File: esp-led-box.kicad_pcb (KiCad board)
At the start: 2 copper layers, 41 x 66 mm, 38 parts, among them J1 Conn_01x03, J2 Conn_01x03_Female, J3 Conn_01x02_Female, Q1 BSS138, U1 MP2307, U2 LM3940, U3 ESP-12F

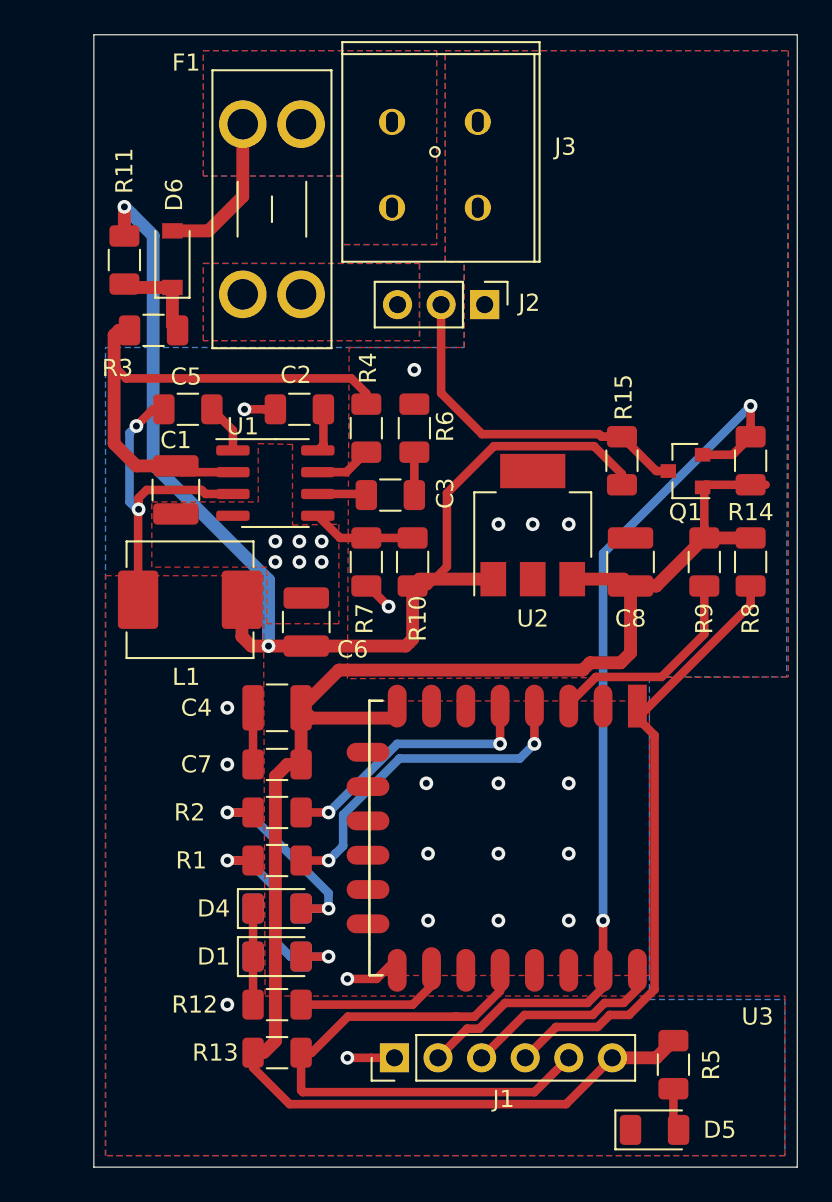
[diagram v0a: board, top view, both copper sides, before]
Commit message: rework fuse holder: use one from aliexpress
https://aliexpress.ru/item/32838425418.html?spm=a2g0s.9042311.0.0.5f9933edQqCEM1 here is the link (it supposed to be used with micro blades fuses)
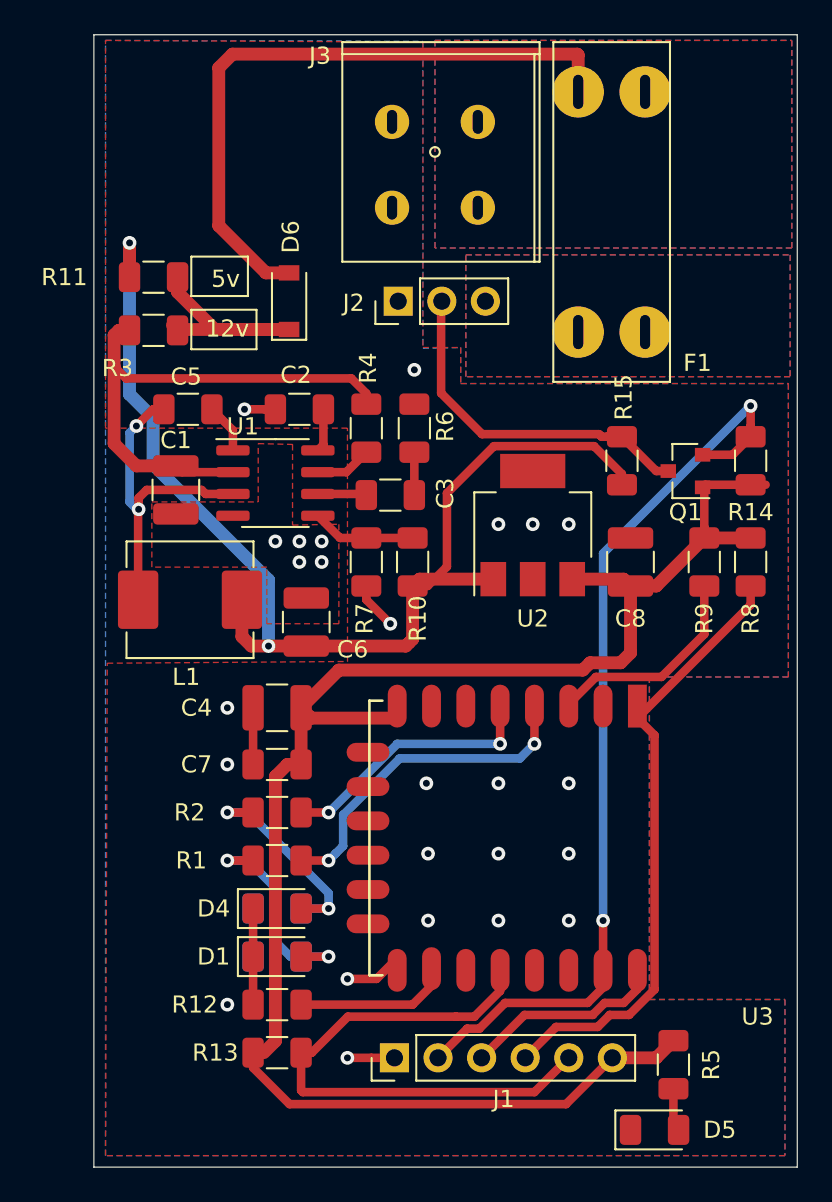
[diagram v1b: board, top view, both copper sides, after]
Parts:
- F1: footprint Fuse:Fuseholder_Blade_Mini_Keystone_3568 -> esp-light-box:fuseholder_blade_common_aliexpress
- moved F1 18.7 mm to (137.7, 60.3)
- moved D6 7.23 mm to (122.4, 55.5)
- moved J2 5.04 mm to (128.8, 55.5), turned to 90 degrees
- moved R11 1.97 mm to (114.5, 54.1), turned to 180 degrees
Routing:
- net VSS: track 9.15 -> 37.9 mm
- net +VDC: track 5.51 -> 15.2 mm
- net +5V: track 70.6 -> 68.7 mm
- net GND: track 18.6 -> 19.7 mm, vias 26 -> 25
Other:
- board text added: "12v"
- board text added: "5v"

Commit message: pcb v0.3 update
- add possibility to use switch instead of dummy resisters
- add micro USB footprint for portable use
- add buttons for RESET and GPIO0 ESP inputs
- make it fancier with components density increased
- add case mountpoints
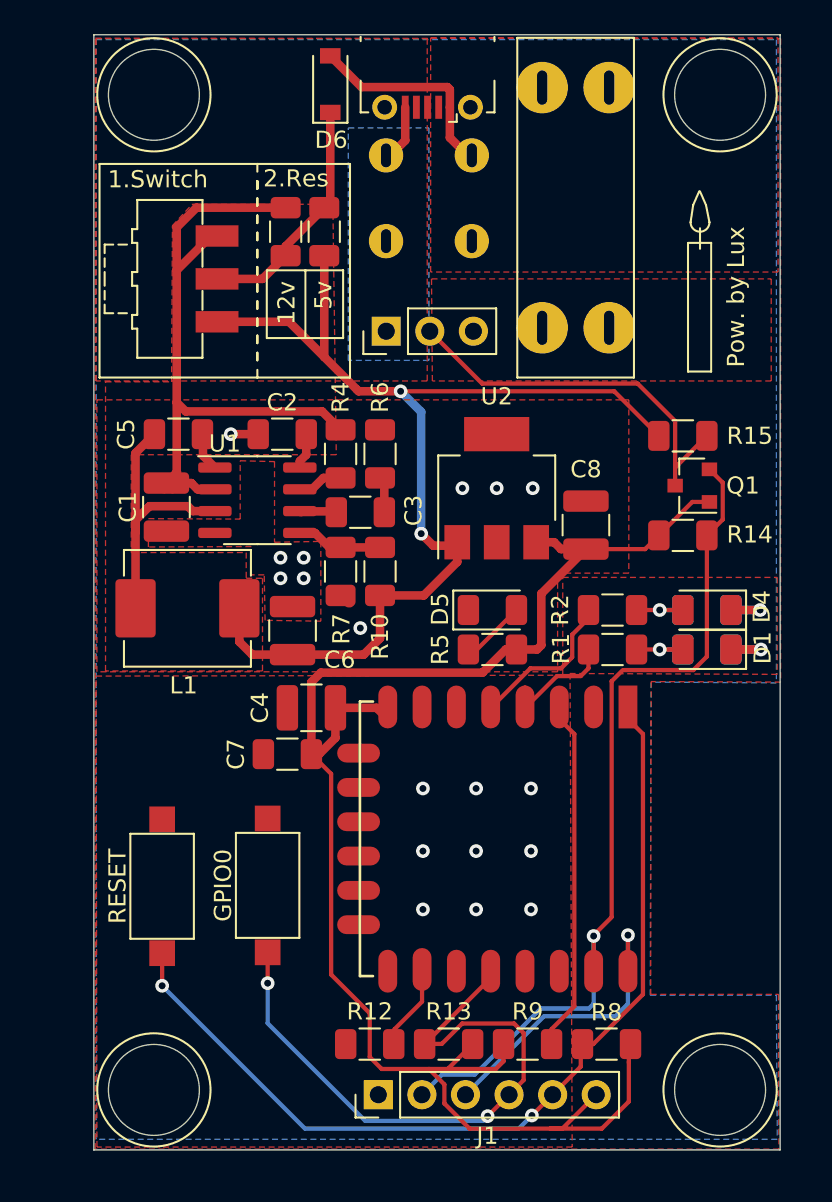
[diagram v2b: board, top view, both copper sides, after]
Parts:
- added GPIO0: SW_Push, Button_Switch_SMD:SW_SPST_CK_RS282G05A3, F.Cu at (121.2, 89.5)
- added J4: USB_B_Micro, Connector_USB:USB_Micro-B_Molex-105017-0001, F.Cu at (130.5, 42.7)
- added REF**: MountingHole_5.3mm_M5, MountingHole:MountingHole_5.3mm_M5, F.Cu at (147.5, 101.5)
- added REF**: MountingHole_5.3mm_M5, MountingHole:MountingHole_5.3mm_M5, F.Cu at (147.5, 43.5)
- added REF**: MountingHole_5.3mm_M5, MountingHole:MountingHole_5.3mm_M5, F.Cu at (114.5, 101.5)
- added REF**: MountingHole_5.3mm_M5, MountingHole:MountingHole_5.3mm_M5, F.Cu at (114.5, 43.5)
- added RESET: SW_Push, Button_Switch_SMD:SW_SPST_CK_RS282G05A3, F.Cu at (115.0, 89.6)
- added SW3: SW_SPDT, Button_Switch_SMD:SW_SPDT_CK-JS102011SAQN, F.Cu at (115.5, 54.2)
- J3: moved to B.Cu
- moved D5 31.7 mm to (134.2, 73.5)
- moved D1 30.8 mm to (146.8, 75.8), turned to 180 degrees
- moved D2 30.8 mm to (146.8, 75.8), turned to 180 degrees
- moved D3 30.5 mm to (146.8, 73.5), turned to 180 degrees
- moved D4 30.5 mm to (146.8, 73.5), turned to 180 degrees
- moved R9 29.9 mm to (136.3, 98.8), turned to 180 degrees
- moved R8 29.3 mm to (140.9, 98.8), turned to 0 degrees
- moved R5 26.4 mm to (134.2, 75.8), turned to 180 degrees
- moved R1 23.1 mm to (141.2, 75.8), turned to 0 degrees
- moved R2 22.8 mm to (141.2, 73.5), turned to 0 degrees
- moved D6 12.9 mm to (124.8, 42.9)
- moved J3 10.6 mm to (135.9, 55.1)
- moved R11 10.3 mm to (124.5, 51.5), turned to 270 degrees
- moved R13 10.0 mm to (131.7, 98.8), turned to 180 degrees
- moved R3 9.61 mm to (122.2, 51.5), turned to 90 degrees
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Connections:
- net Net-(C1-Pad1) renamed +12V
- J1 pad 4: /RESET -> /GPIO0
- J1 pad 5: /GPIO0 -> /RESET
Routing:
- net VSS: track 37.9 -> 12.4 mm
- net /RESET: track 35.9 -> 53.7 mm, vias 0 -> 2
- net /GREEN_LED: track 19.0 -> 8.25 mm, vias 2 -> 0
- net +12V: track 30.9 -> 40.9 mm
- net Net-(D3-Pad2): track 13.4 -> 4.05 mm, vias 2 -> 1
- net Net-(D1-Pad2): track 13.2 -> 4.05 mm, vias 2 -> 1
- net GND: track 19.7 -> 12.1 mm, vias 25 -> 20
- net Net-(R9-Pad1): track 13.2 -> 19.9 mm
- net /GPIO0: track 33.7 -> 39.3 mm, vias 0 -> 2
- net /TXD: track 12.5 -> 17.1 mm, vias 0 -> 1
- net /RED_LED: track 14.8 -> 10.7 mm, vias 2 -> 0
- net Net-(R12-Pad2): track 9.66 -> 5.61 mm
- net +3V3: track 99.2 -> 95.5 mm
- net +5V: track 68.7 -> 65.5 mm
- net Net-(C5-Pad1): track 19.0 -> 16.4 mm, vias 2 -> 0
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- added copper zone on F.Cu, net (none)
- removed copper zone on B.Cu, net Net-(F1-Pad1)
- removed copper zone on B.Cu, net VSS
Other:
- board size 41 x 66 mm -> 40 x 65 mm
- board text added: "1.Switch"
- board text added: "2.Res"
- board text added: "Pow. by Lux"

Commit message: my new version is coming
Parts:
- removed D2, D3, D4, D5: LED, LED_SMD:LED_1206_3216Metric
- removed D6: D, Diode_SMD:D_SOD-123
- removed GPIO0, RESET: SW_Push, Button_Switch_SMD:SW_SPST_CK_RS282G05A3
- removed the REF** at (147.5, 101.5)
- removed the REF** at (147.5, 43.5)
- removed the REF** at (114.5, 101.5)
- removed the REF** at (114.5, 43.5)
- removed SW3: SW_SPDT, Button_Switch_SMD:SW_SPDT_CK-JS102011SAQN
- added C10: 1uF, Capacitor_SMD:C_0402_1005Metric, F.Cu at (163.4, 68.8)
- added C11: 220u, Capacitor_SMD:CP_Elec_6.3x7.7, F.Cu at (138.4, 82.8)
- added C12: 100nF, Capacitor_SMD:C_0402_1005Metric, F.Cu at (162.4, 68.8)
- added C9: 10u, Capacitor_SMD:C_0603_1608Metric, F.Cu at (157.4, 60.8)
- added IC1: CP2105-F01-GMR, CP2105-F01-GMR:QFN50P400X400X80-25N-D, F.Cu at (160.4, 66.3)
- added J5: Conn_01x02, Connector_PinHeader_2.54mm:PinHeader_1x02_P2.54mm_Vertical, F.Cu at (128.2, 105.2)
- added Q2: Q_PMOS_DGS, Package_TO_SOT_SMD:SOT-23-6, F.Cu at (161.0, 85.3)
- added Q3: Q_PMOS_DGS, Package_TO_SOT_SMD:SOT-23-6, F.Cu at (154.2, 99.0)
- added Q4: S8050, Package_TO_SOT_SMD:SOT-23, F.Cu at (157.1, 70.0)
- added Q5: S8050, Package_TO_SOT_SMD:SOT-23, F.Cu at (153.6, 70.0)
- added Q6: Q_PMOS_DGS, Package_TO_SOT_SMD:SOT-23-6, F.Cu at (153.6, 66.0)
- added Q7: BSS138, Package_TO_SOT_SMD:SOT-23, F.Cu at (138.8, 96.2)
- added Q8: Q_PMOS_DGS, Package_TO_SOT_SMD:TO-252-2, F.Cu at (140.6, 73.6)
- added Q9: Q_NMOS, Package_TO_SOT_SMD:SOT-23, F.Cu at (145.7, 64.2)
- added R16: 20K, Resistor_SMD:R_0402_1005Metric, F.Cu at (157.1, 73.7)
- added R17: 12K, Resistor_SMD:R_0402_1005Metric, F.Cu at (156.9, 67.4)
- added R18: 12K, Resistor_SMD:R_0402_1005Metric, F.Cu at (156.9, 64.5)
- added R21: 4.7K, Resistor_SMD:R_0402_1005Metric, F.Cu at (163.4, 66.0)
- added R22: 300, Resistor_SMD:R_0402_1005Metric, F.Cu at (156.9, 66.5)
- added R23: 300, Resistor_SMD:R_0402_1005Metric, F.Cu at (156.9, 65.5)
- added R24: 10K, Resistor_SMD:R_0402_1005Metric, F.Cu at (138.3, 98.5)
- added R25: 10K, Resistor_SMD:R_0402_1005Metric, F.Cu at (141.5, 95.0)
- added REF**: MountingHole_2.2mm_M2, MountingHole:MountingHole_2.2mm_M2, F.Cu at (162.0, 60.5)
- added REF**: MountingHole_2.2mm_M2, MountingHole:MountingHole_2.2mm_M2, F.Cu at (128.0, 60.5)
- added REF**: MountingHole_2.2mm_M2, MountingHole:MountingHole_2.2mm_M2, F.Cu at (128.0, 119.5)
- added REF**: MountingHole_2.2mm_M2, MountingHole:MountingHole_2.2mm_M2, F.Cu at (162.0, 119.5)
- added U4: LM3940, Package_TO_SOT_SMD:SOT-223-3_TabPin2, F.Cu at (147.1, 97.2)
- C1: value 10uF/25V -> 10u/25V; footprint Capacitor_SMD:C_1210_3225Metric -> Capacitor_SMD:C_1206_3216Metric
- C2: value 0.1uF -> 10uF; footprint Capacitor_SMD:C_1206_3216Metric -> Capacitor_Tantalum_SMD:CP_EIA-3216-18_Kemet-A
- C3: value 3.9nF -> 100nF; footprint Capacitor_SMD:C_1206_3216Metric -> Capacitor_SMD:C_0402_1005Metric
- C4: value 10uF -> 100nF; footprint Capacitor_SMD:C_1210_3225Metric -> Capacitor_SMD:C_0402_1005Metric
- C5: value 10nF -> 3.9nF; footprint Capacitor_SMD:C_1206_3216Metric -> Capacitor_SMD:C_0402_1005Metric
- C6: value 22uF/6.3V -> 10nF; footprint Capacitor_SMD:C_1210_3225Metric -> Capacitor_SMD:C_0402_1005Metric
- C7: value 100nF -> 47uF/6.3V
- C8: footprint Capacitor_SMD:C_1210_3225Metric -> Capacitor_Tantalum_SMD:CP_EIA-3216-18_Kemet-A
- D1: value LED -> 2.4V; footprint LED_SMD:LED_1206_3216Metric -> Diode_SMD:D_SOD-323
- J1: value Conn_01x03 -> Conn_01x04; footprint Connector_PinHeader_2.54mm:PinHeader_1x06_P2.54mm_Vertical -> Connector_PinHeader_2.54mm:PinHeader_1x04_P2.54mm_Vertical
- J2: value Conn_01x03_Female -> USB_B_Micro; footprint Connector_PinHeader_2.54mm:PinHeader_1x03_P2.54mm_Vertical -> Connector_USB:USB_Micro-B_Molex-105017-0001
- J3: value Conn_01x02_Female -> Conn_01x03_Female; footprint esp-light-box:WG235-2P -> esp-light-box:SolderWire_1x03_2.5x6; moved to F.Cu
- J4: value USB_B_Micro -> Conn_01x03_Female; footprint Connector_USB:USB_Micro-B_Molex-105017-0001 -> esp-light-box:SolderWire_1x03_2.5x6
- L1: footprint Inductor_SMD:L_Abracon_ASPI-0630LR -> Inductor_SMD:L_Sunlord_MWSA0518_5.4x5.2mm
- Q1: value BSS138 -> Q_NMOS
- R1, R2: value 120 -> 1M; footprint Resistor_SMD:R_1206_3216Metric -> Resistor_SMD:R_0402_1005Metric
- R10, R12, R4: footprint Resistor_SMD:R_1206_3216Metric -> Resistor_SMD:R_0402_1005Metric
- R11: value 0 -> 360; footprint Resistor_SMD:R_1206_3216Metric -> Resistor_SMD:R_1210_3225Metric
- R13: value 10K -> 24K; footprint Resistor_SMD:R_1206_3216Metric -> Resistor_SMD:R_0603_1608Metric
- R14: footprint Resistor_SMD:R_1206_3216Metric -> Resistor_SMD:R_0603_1608Metric
- R15: value 10K -> 20K; footprint Resistor_SMD:R_1206_3216Metric -> Resistor_SMD:R_0402_1005Metric
- R3: value 0 -> 10K; footprint Resistor_SMD:R_1206_3216Metric -> Resistor_SMD:R_0402_1005Metric
- R5: value 120 -> 20K; footprint Resistor_SMD:R_1206_3216Metric -> Resistor_SMD:R_0603_1608Metric
- R6: value 6.8K -> 300; footprint Resistor_SMD:R_1206_3216Metric -> Resistor_SMD:R_0805_2012Metric
- R7: value 10K/1% -> 20K; footprint Resistor_SMD:R_1206_3216Metric -> Resistor_SMD:R_0603_1608Metric
- R8: value 10K -> 6.8K; footprint Resistor_SMD:R_1206_3216Metric -> Resistor_SMD:R_0402_1005Metric
- R9: value 10K -> 10K/1%; footprint Resistor_SMD:R_1206_3216Metric -> Resistor_SMD:R_0402_1005Metric
- U2: value LM3940 -> ESP-12F; footprint Package_TO_SOT_SMD:SOT-223-3_TabPin2 -> RF_Module:ESP-12E
- U3: value ESP-12F -> LM211; footprint ESP8266:ESP-12E -> Package_SO:SOIC-8-1EP_3.9x4.9mm_P1.27mm_EP2.29x3mm
- moved C5 57.1 mm to (159.7, 99.9), turned to 270 degrees
- moved R3 52.7 mm to (138.2, 101.7), turned to 270 degrees
- moved R4 50.1 mm to (160.8, 99.9), turned to 90 degrees
- moved C1 49.5 mm to (159.2, 90.3), turned to 180 degrees
- moved U1 48.1 mm to (159.6, 95.1), turned to 270 degrees
- moved C3 47.7 mm to (161.8, 99.9), turned to 270 degrees
- moved J4 47.4 mm to (138.5, 89.5), turned to 0 degrees
- moved U2 46.6 mm to (144.4, 111.9), turned to 270 degrees
- moved R11 43.2 mm to (160.7, 74.8), turned to 0 degrees
- moved C6 42.4 mm to (162.1, 90.4), turned to 270 degrees
- moved L1 41.1 mm to (155.6, 86.2), turned to 180 degrees
- moved C2 40.8 mm to (135.3, 101.8), turned to 0 degrees
- moved R10 40.7 mm to (156.6, 99.9), turned to 270 degrees
- moved J1 36.0 mm to (161.8, 112.8), turned to 180 degrees
- moved R13 35.4 mm to (162.1, 80.5), turned to 90 degrees
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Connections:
- C2 pad 1: Net-(C2-Pad1) -> +3V3
- C3 pad 2: Net-(C3-Pad2) -> GND
- C6 pad 1: +5V -> Net-(C6-Pad1)
- C6 pad 2: GND -> Net-(C6-Pad2)
- C7 pad 1: +3V3 -> /BUCK_5V
- D1 pad 1: GND -> Net-(D1-Pad1)
- D1 pad 2: Net-(D1-Pad2) -> GND
- F1 pad 1: Net-(F1-Pad1) -> /DC_VDD
- F1 pad 2: VSS -> VDD
- J1 pad 1: GND -> /GPIO0
- J1 pad 2: /RXD|CONTROL -> /TXD
- J1 pad 3: /TXD -> /RXD
- J1 pad 4: /GPIO0 -> /RESET
- J2 pad 1: GND -> VBUS
- J2 pad 2: Net-(J2-Pad2) -> /D-
- J2 pad 3: Net-(F1-Pad1) -> /D+
- J3 pad 1: GND -> VDC
- J3 pad 2: VSS -> VDC
- J4 pad 1: VSS -> GND
- J4 pad 3: Net-(J4-Pad3) -> VDD
- L1 pad 1: Net-(C5-Pad1) -> Net-(C6-Pad1)
- L1 pad 2: +5V -> /BUCK_5V
- Q1 pad 1: +3V3 -> /~12V_SEL
- Q1 pad 2: /RXD|CONTROL -> GND
- Q1 pad 3: Net-(J2-Pad2) -> /~5V_SEL
- R1 pad 1: /GREEN_LED -> VBUS
- R1 pad 2: Net-(D1-Pad2) -> GND
- R10 pad 1: +5V -> /BUCK_5V
- R11 pad 1: +VDC -> Net-(D1-Pad1)
- R11 pad 2: +5V -> VDD
- R12 pad 1: GND -> Net-(R12-Pad1)
- R12 pad 2: Net-(R12-Pad2) -> GND
- R13 pad 1: +3V3 -> VDD
- R13 pad 2: /GPIO0 -> Net-(R13-Pad2)
- R14 pad 1: /RXD|CONTROL -> Net-(R13-Pad2)
- R14 pad 2: +3V3 -> GND
- R15 pad 1: Net-(J2-Pad2) -> VDD
- R15 pad 2: +5V -> /~12V_SEL
- R2 pad 1: /RED_LED -> VDC
- R2 pad 2: Net-(D3-Pad2) -> GND
- R3 pad 1: +VDC -> +3V3
- R3 pad 2: +12V -> Net-(R3-Pad2)
- R5 pad 1: +3V3 -> VBUS
- R5 pad 2: Net-(D5-Pad2) -> /~VDC_SEL
- R6 pad 1: Net-(C3-Pad2) -> VDC
- R6 pad 2: GND -> /VDC_ON
- R7 pad 1: Net-(R10-Pad2) -> VDC
- R7 pad 2: GND -> Net-(Q9-Pad1)
- R8 pad 1: /RESET -> Net-(C5-Pad2)
- R8 pad 2: +3V3 -> GND
- R9 pad 1: Net-(R9-Pad1) -> Net-(R10-Pad2)
- R9 pad 2: +3V3 -> GND
- U1 pad 1: Net-(C5-Pad2) -> Net-(C6-Pad2)
- U1 pad 3: Net-(C5-Pad1) -> Net-(C6-Pad1)
- U1 pad 6: Net-(C3-Pad1) -> Net-(C5-Pad1)
- U1 pad 8: Net-(C2-Pad1) -> Net-(C3-Pad1)
- U2 pad 1: +5V -> /RESET
- U2 pad 2: GND -> Net-(U2-Pad2)
- U2 pad 3: +3V3 -> Net-(R3-Pad2)
- U3 pad 1: /RESET -> GND
- U3 pad 2: Net-(U3-Pad2) -> Net-(R13-Pad2)
- U3 pad 3: Net-(R9-Pad1) -> Net-(D1-Pad1)
- U3 pad 4: /GREEN_LED -> GND
- U3 pad 5: /RED_LED -> Net-(U3-Pad5)
- U3 pad 6: Net-(U3-Pad6) -> Net-(U3-Pad5)
- U3 pad 7: Net-(U3-Pad7) -> /~12V_SEL
- U3 pad 8: +3V3 -> VDD
- U3 pad 9: GND -> (no net)
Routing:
- net /RXD: track 0.00 -> 76.9 mm, vias 0 -> 4
- net +3V3: track 95.5 -> 33.5 mm, vias 0 -> 1
- net /TXD: track 17.1 -> 74.6 mm, vias 1 -> 2
- net /RXD|CONTROL: track 52.2 -> 0.00 mm, vias 1 -> 0
- net /~5V_SEL: track 0.00 -> 51.2 mm
- net +5V: track 65.5 -> 17.4 mm, vias 2 -> 0
- net /GPIO0: track 39.3 -> 77.2 mm
- net /~12V_SEL: track 0.00 -> 37.5 mm, vias 0 -> 2
- net /LED_CTRL: track 0.00 -> 35.3 mm
- net VDD: track 0.00 -> 35.2 mm, vias 0 -> 25
- net VBUS: track 0.00 -> 30.4 mm
- net /DC_5V: track 0.00 -> 24.5 mm
- net Net-(J2-Pad2): track 22.8 -> 0.00 mm
- net +12V: track 40.9 -> 18.3 mm
- net /~VDC_SEL: track 0.00 -> 22.3 mm
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- added copper zone on B.Cu, net (none)
- added copper zone on F.Cu, net +12V
- added copper zone on F.Cu, net /BUCK_5V
- added copper zone on B.Cu, net /DC_VDD
- added copper zone on F.Cu, net /DC_VDD
- added copper zone on F.Cu, net Net-(C6-Pad1)
- added copper zone on B.Cu, net VDC
- added copper zone on F.Cu, net VDC
- added copper zone on B.Cu, net VDD
- added copper zone on F.Cu, net VDD
- removed copper zone on F.Cu, net Net-(F1-Pad1)
- removed copper zone on F.Cu, net VSS
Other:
- board size 40 x 65 mm -> 39 x 64 mm
- net class Default: clearance 0.2 -> 0.127; trace_width 0.25 -> 0.127
- net class Digital Power added: clearance 0.127, trace_width 0.254, via_dia 0.8, via_drill 0.4
- net class Signal added: clearance 0.127, trace_width 0.254, via_dia 0.8, via_drill 0.4
- rule trace_clearance: 0.2 -> 0.127
- rule trace_min: 0.2 -> 0.127
- rule via_min_drill: 0.3 -> 0.2
- board text removed: "1.Switch"
- board text removed: "12v"
- board text removed: "2.Res"
- board text removed: "5v"

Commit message: another kek
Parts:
- removed REF** (x4): MountingHole_2.2mm_M2, MountingHole:MountingHole_2.2mm_M2
- moved J1 77.2 mm to (86.4, 96.9), turned to 0 degrees
- moved C6 75.9 mm to (86.6, 82.4)
- moved C7 75.9 mm to (79.1, 82.3)
- moved C9 75.9 mm to (81.9, 52.8)
- moved Q5 75.9 mm to (78.1, 62.0)
- moved R13 75.9 mm to (86.6, 72.5)
- moved R2 75.9 mm to (69.7, 52.5)
- moved R5 75.9 mm to (74.1, 58.9)
- moved U3 75.9 mm to (80.6, 71.3)
- moved C1 75.9 mm to (83.7, 82.3)
- moved C10 75.9 mm to (87.9, 60.8)
- moved C11 75.9 mm to (62.9, 74.8)
- moved C12 75.9 mm to (86.9, 60.8)
- moved C2 75.9 mm to (59.9, 93.8)
- moved C4 75.9 mm to (58.6, 92.3)
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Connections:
- J1 pad 2: /TXD -> /RESET
- J1 pad 4: /RESET -> /TXD
- J5 pad 1: +3V3 -> GND
- J5 pad 2: GND -> +3V3
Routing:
- net +3V3: track 33.5 -> 24.8 mm, vias 1 -> 2
- net /V_IO: track 9.31 -> 15.0 mm
- net /RESET: track 59.5 -> 65.2 mm, vias 4 -> 0
- net /~5V_SEL: track 51.2 -> 47.3 mm, vias 0 -> 3
- net GND: track 30.6 -> 26.8 mm
- net VDD: track 35.2 -> 37.4 mm, vias 25 -> 27
- net /GPIO0: track 77.2 -> 79.5 mm, vias 2 -> 0
- net /TXD: track 74.6 -> 73.0 mm, vias 2 -> 1
- net /RXD: track 76.9 -> 75.5 mm, vias 4 -> 3
- net /D-: track 14.1 -> 13.0 mm
- net /D+: track 15.2 -> 14.2 mm
- added copper zone on B.Cu, net +3V3
- added copper zone on F.Cu, net +3V3
- added copper zone on F.Cu, net +5V
- removed copper zone on B.Cu, net (none)
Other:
- outline, holes or cut-outs redrawn

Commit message: another kek hehe
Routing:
- net /TXD: track 73.0 -> 90.7 mm, vias 1 -> 2
- net /RXD: track 75.5 -> 89.9 mm, vias 3 -> 2
- net Net-(R12-Pad1): track 19.4 -> 22.5 mm
- net /GPIO0: track 79.5 -> 79.0 mm

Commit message: finally we are done
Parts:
- removed the C10 at (87.9, 60.8)
- removed the C2 at (59.9, 93.8)
- removed the C5 at (84.2, 91.9)
- removed R24: 10K, Resistor_SMD:R_0402_1005Metric
- removed the U2 at (68.9, 103.9)
- removed the U4 at (71.6, 89.3)
- added C11: 1uF, Capacitor_SMD:C_0402_1005Metric, F.Cu at (87.9, 60.8)
- added C3: 3.9nF, Capacitor_SMD:C_0402_1005Metric, F.Cu at (84.2, 91.9)
- added C6: 100nF, Capacitor_SMD:C_0402_1005Metric, F.Cu at (56.9, 93.4)
- added R22: 10K, Resistor_SMD:R_0402_1005Metric, F.Cu at (56.7, 86.8)
- added REF**: TestPoint_Pad_4.0x4.0mm, TestPoint:TestPoint_Pad_4.0x4.0mm, B.Cu at (84.2, 71.3)
- added REF**: MountingHole_2.2mm_M2, MountingHole:MountingHole_2.2mm_M2, F.Cu at (52.5, 52.5)
- added REF**: MountingHole_2.2mm_M2, MountingHole:MountingHole_2.2mm_M2, F.Cu at (86.5, 52.5)
- added REF**: MountingHole_2.2mm_M2, MountingHole:MountingHole_2.2mm_M2, F.Cu at (86.5, 111.5)
- added REF**: MountingHole_2.2mm_M2, MountingHole:MountingHole_2.2mm_M2, F.Cu at (52.5, 111.5)
- added TP1: GND, TestPoint:TestPoint_Pad_1.0x1.0mm, F.Cu at (87.8, 63.7)
- added TP2: GND, TestPoint:TestPoint_Pad_1.0x1.0mm, F.Cu at (51.3, 56.4)
- added TP3: ~12V_SEL, TestPoint:TestPoint_Pad_D1.0mm, F.Cu at (73.5, 88.1)
- added TP4: ~5V_SEL, TestPoint:TestPoint_Pad_D1.0mm, F.Cu at (73.5, 90.5)
- added U1: LM3940, Package_TO_SOT_SMD:SOT-223-3_TabPin2, F.Cu at (65.3, 90.9)
- added U3: ESP-12F, RF_Module:ESP-12E, F.Cu at (68.9, 103.9)
- C1: value 10u/25V -> 22u/25V; footprint Capacitor_SMD:C_1206_3216Metric -> Capacitor_SMD:C_0805_2012Metric
- C4: value 100nF -> 100uF; footprint Capacitor_SMD:C_0402_1005Metric -> Capacitor_Tantalum_SMD:CP_EIA-3528-21_Kemet-B
- C7: value 47uF/6.3V -> 22uF 6.3V; footprint Capacitor_SMD:C_1206_3216Metric -> Capacitor_SMD:C_0603_1608Metric
- C8: value 33uF -> 22uF 6.3V; footprint Capacitor_Tantalum_SMD:CP_EIA-3216-18_Kemet-A -> Capacitor_SMD:C_0603_1608Metric
- D1: value 2.4V -> 5.6V; footprint Diode_SMD:D_SOD-323 -> Diode_SMD:D_MiniMELF
- Q1: renamed from Q9; value Q_NMOS -> 2N7002
- Q2: renamed from Q1; value Q_NMOS -> 2N7002
- Q8: renamed from Q7; value BSS138 -> 2N7002
- R11: value 360 -> 1K; footprint Resistor_SMD:R_1210_3225Metric -> Resistor_SMD:R_0603_1608Metric
- R13: value 24K -> 22K; footprint Resistor_SMD:R_0603_1608Metric -> Resistor_SMD:R_0402_1005Metric
- R14: value 10K -> 20K; footprint Resistor_SMD:R_0603_1608Metric -> Resistor_SMD:R_0402_1005Metric
- R15: value 20K -> 10K
- moved R15 47.4 mm to (55.1, 107.2), turned to 90 degrees
- moved R12 44.8 mm to (84.8, 73.7)
- moved C8 14.4 mm to (78.8, 83.8), turned to 0 degrees
- moved R10 7.65 mm to (70.3, 93.5)
- moved R14 5.72 mm to (81.6, 67.9), turned to 180 degrees
- moved Q8 4.37 mm to (59.0, 87.3)
- moved R23 4.12 mm to (61.9, 86.4)
- moved R13 1.90 mm to (84.8, 71.8), turned to 270 degrees
- moved R11 1.76 mm to (83.5, 67.0), turned to 90 degrees
- moved D1 1.48 mm to (85.4, 68.2), turned to 90 degrees
- moved C4 0.50 mm to (59.0, 92.0), turned to 90 degrees
- moved C7 0.30 mm to (78.8, 82.3)
- renumbered C12 to C10, C11 to C12, C3 to C2, C6 to C5, J5 to J2, J2 to J3, J3 to J4, J4 to J5, Q2 to Q3, Q3 to Q4, Q4 to Q5, Q5 to Q6, Q6 to Q7, Q8 to Q9, R3 to R10, R21 to R19, R22 to R20, R23 to R21, R25 to R23, R4 to R3, R5 to R4, R6 to R5, R7 to R6, R8 to R7, R9 to R8, R10 to R9, U1 to U2, U3 to U4
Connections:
- C8 pad 1: +3V3 -> /BUCK_5V
- R12 pad 1: Net-(R12-Pad1) -> VDD
- R12 pad 2: GND -> Net-(R12-Pad2)
- R13 pad 1: VDD -> Net-(R12-Pad2)
- R13 pad 2: Net-(R13-Pad2) -> GND
- R14 pad 1: Net-(R13-Pad2) -> VDD
- R14 pad 2: GND -> /~12V_SEL
- R15 pad 1: VDD -> Net-(R15-Pad1)
- R15 pad 2: /~12V_SEL -> GND
- U4 pad 2: Net-(R13-Pad2) -> Net-(R12-Pad2)
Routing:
- net Net-(R12-Pad1): track 22.5 -> 0.00 mm
- net +5V: track 17.4 -> 4.46 mm
- net /LED_CTRL: track 35.3 -> 47.6 mm
- net Net-(R15-Pad1): track 0.00 -> 11.6 mm
- net +3V3: track 24.8 -> 31.0 mm, vias 2 -> 0
- net VDD: track 37.4 -> 32.5 mm, vias 27 -> 25
- net Net-(R12-Pad2): track 0.00 -> 4.59 mm
- net Net-(R10-Pad2): track 7.49 -> 3.11 mm
- net /~5V_SEL: track 47.3 -> 51.6 mm, vias 3 -> 2
- net /~12V_SEL: track 37.5 -> 41.7 mm, vias 2 -> 4
- net Net-(R13-Pad2): track 3.61 -> 0.00 mm
- net Net-(J5-Pad2): track 9.10 -> 7.37 mm
- net Net-(D1-Pad1): track 5.75 -> 6.33 mm, vias 0 -> 1
- net GND: track 26.8 -> 26.4 mm, vias 122 -> 126
- removed copper zone on B.Cu, net +3V3

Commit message: ... dont say anything
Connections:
- TP1 pad 1: (no net) -> GND
- TP2 pad 1: (no net) -> GND
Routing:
- net GND: track 26.4 -> 23.0 mm
- net /V_IO: track 15.1 -> 15.9 mm

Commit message: ~_~
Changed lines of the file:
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@@
       (pts
         (xy 75.85 71.225) (xy 62.95 71.225001) (xy 62.95 67.300002) (xy 68.5 67.3) (xy 68.5 60.3)
-        (xy 75.85 60.225)
+        (xy 75.85 60.3)
       )
     )
